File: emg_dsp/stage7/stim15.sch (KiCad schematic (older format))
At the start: 41 parts, among them U31 10X100, U32 MCP4017, U33 6533-CONN, U34 GT12MABE, U35 IL715-3, U36 IL715-3, U37 IL715-3, U38 IL715-3, U39 IL715-3, U40 IL715-3, U41 IL715-3, U42 IL715-3

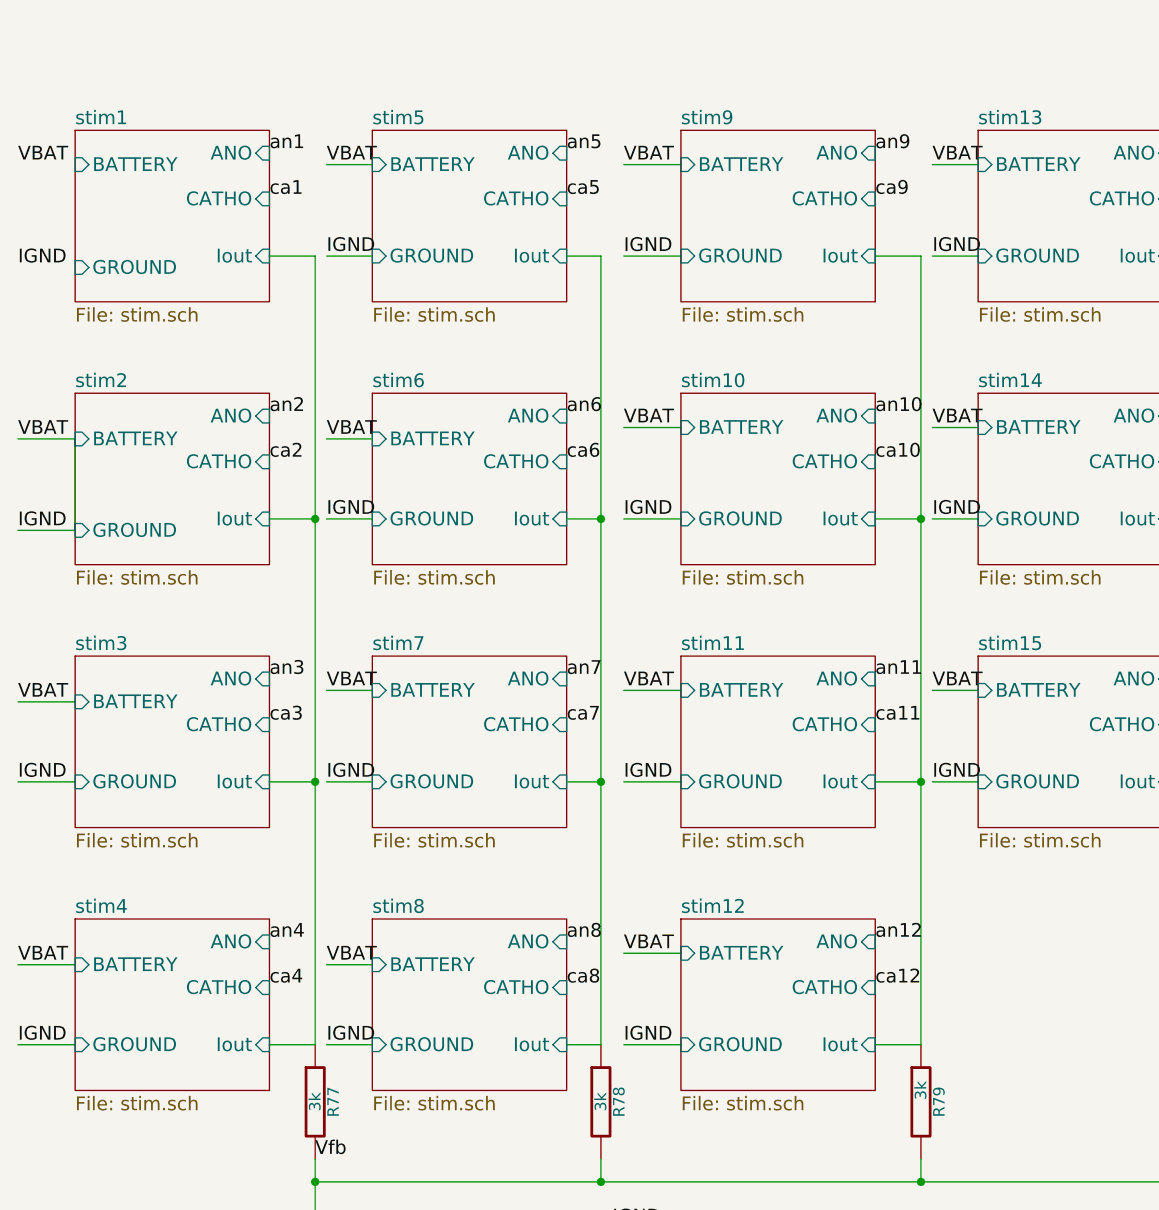
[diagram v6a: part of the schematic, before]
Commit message: finally fixed the VBAT = IGND issue - did so by using wires rather than labels on the inputs to the individual instances of stim.sch yea, that doesn't make sense -should work either way - but ok!
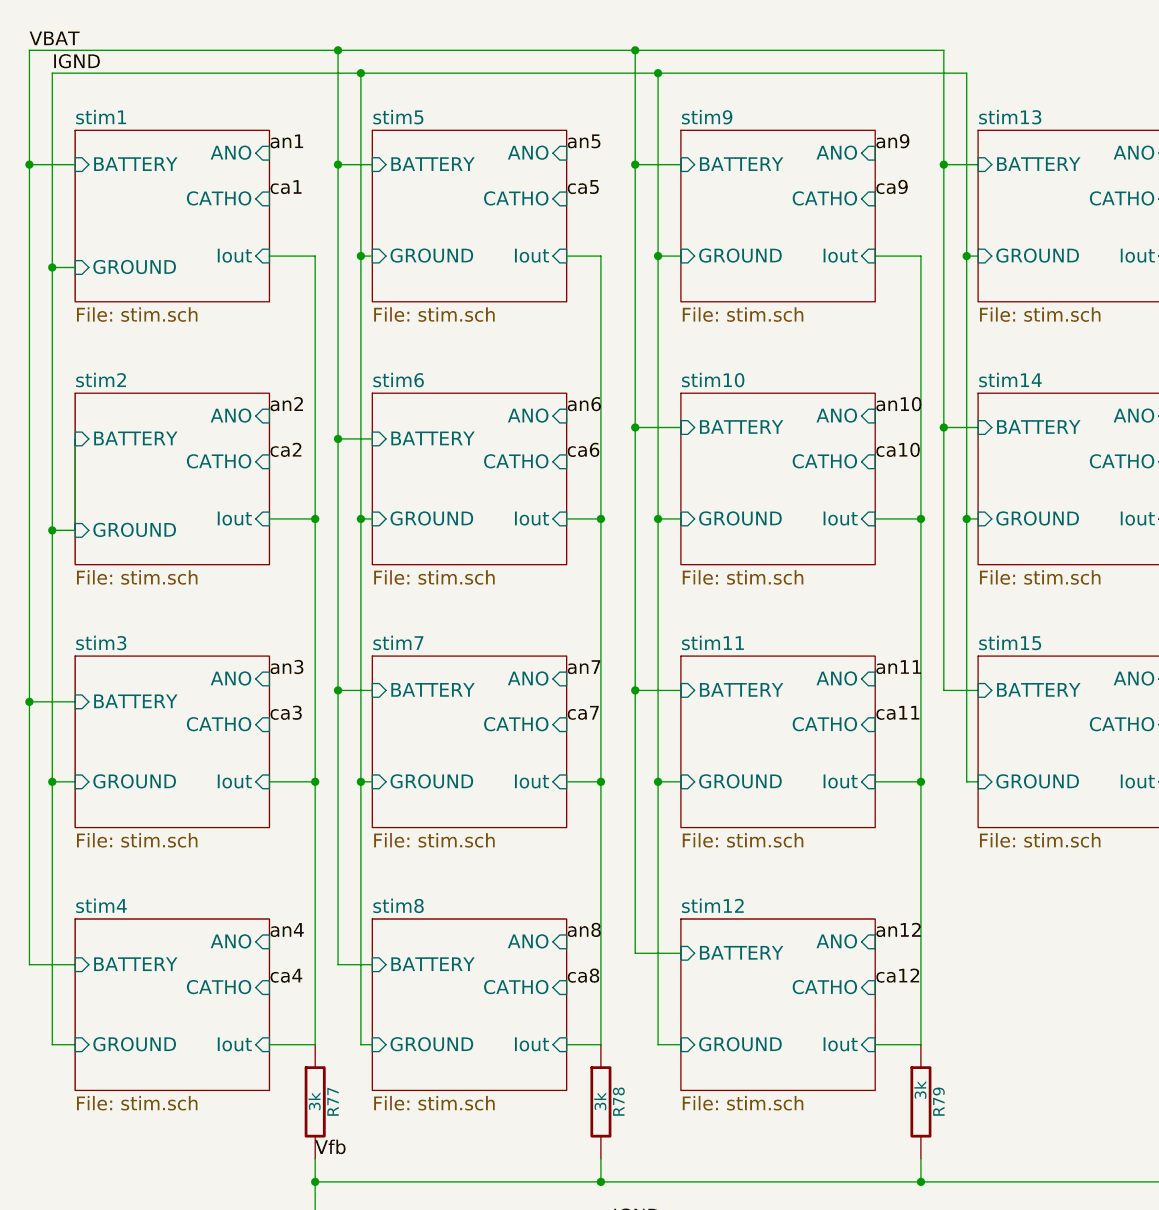
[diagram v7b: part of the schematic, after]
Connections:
- wire segments 259 -> 270
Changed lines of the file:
@@
-EESchema Schematic File Version 2  date Mon 24 Jan 2011 02:31:03 PM EST
+EESchema Schematic File Version 2  date Mon 24 Jan 2011 03:09:10 PM EST
 LIBS:power
 LIBS:device
@@
 Comment4 ""
 $EndDescr
+Text Label 800  1100 0    60   ~ 0
+IGND
+Text Label 700  1000 0    60   ~ 0
+VBAT
+Connection ~ 2050 1500
+Connection ~ 2050 1000
+Wire Wire Line
+	2050 1000 2050 5000
+Connection ~ 3350 1500
+Connection ~ 3350 1000
+Wire Wire Line
+	3350 1000 3350 4950
+Connection ~ 800  1950
+Connection ~ 4800 1900
+Wire Wire Line
+	4800 1100 4800 4200
+Wire Wire Line
+	4800 1100 800  1100
+Wire Wire Line
+	800  1100 800  5350
+Connection ~ 4800 3050
+Wire Wire Line
+	4850 3050 4800 3050
+Connection ~ 4700 2650
+Wire Wire Line
+	4850 2650 4700 2650
+Connection ~ 3450 3050
+Wire Wire Line
+	3550 3050 3450 3050
+Wire Wire Line
+	3550 5350 3450 5350
+Wire Wire Line
+	3450 1900 3550 1900
+Connection ~ 3350 2650
+Wire Wire Line
+	3550 2650 3350 2650
+Wire Wire Line
+	3350 1500 3550 1500
+Connection ~ 2150 4200
+Wire Wire Line
+	2200 4200 2150 4200
+Connection ~ 2050 2700
+Wire Wire Line
+	2200 2700 2050 2700
+Wire Wire Line
+	2050 5000 2200 5000
+Wire Wire Line
+	2050 1500 2200 1500
+Connection ~ 800  3100
+Wire Wire Line
+	800  3100 900  3100
+Wire Wire Line
+	800  5350 900  5350
+Wire Wire Line
+	800  1950 900  1950
 Connection ~ 7550 3000
 Wire Wire Line
@@
 Wire Wire Line
 	5000 6800 4750 6800
-Wire Wire Line
-	650  2700 900  2700
-Wire Wire Line
-	650  4200 900  4200
-Wire Wire Line
-	650  5350 900  5350
-Wire Wire Line
-	2200 5000 2000 5000
-Wire Wire Line
-	2200 3800 2000 3800
-Wire Wire Line
-	2200 2700 2000 2700
-Wire Wire Line
-	2200 1500 2000 1500
-Wire Wire Line
-	3550 4950 3300 4950
-Wire Wire Line
-	3550 3800 3300 3800
-Wire Wire Line
-	3550 2650 3300 2650
-Wire Wire Line
-	3550 1500 3300 1500
-Wire Wire Line
-	4850 1900 4650 1900
-Wire Wire Line
-	4850 3050 4650 3050
-Wire Wire Line
-	4850 4200 4650 4200
 Wire Wire Line
 	2000 6700 2200 6700
@@
 	3250 6550 3050 6550
 Wire Wire Line
-	900  2700 900  3100
-Wire Wire Line
-	4850 3800 4650 3800
-Wire Wire Line
-	4850 2650 4650 2650
-Wire Wire Line
-	4850 1500 4650 1500
-Wire Wire Line
-	3550 1900 3300 1900
-Wire Wire Line
-	3550 3050 3300 3050
-Wire Wire Line
-	3550 4200 3300 4200
-Wire Wire Line
-	3550 5350 3300 5350
-Wire Wire Line
-	2200 1900 2000 1900
-Wire Wire Line
-	2200 3050 2000 3050
-Wire Wire Line
-	2200 4200 2000 4200
-Wire Wire Line
-	2200 5350 2000 5350
-Wire Wire Line
-	900  5000 650  5000
-Wire Wire Line
-	900  3850 650  3850
-Wire Wire Line
-	900  3100 650  3100
+	900  3100 900  2700
 Wire Wire Line
 	4750 7350 4750 7100
@@
 Connection ~ 7750 8100
 Connection ~ 7950 8100
+Wire Wire Line
+	700  1500 900  1500
+Wire Wire Line
+	900  5000 700  5000
+Wire Wire Line
+	900  4200 800  4200
+Connection ~ 800  4200
+Wire Wire Line
+	900  3850 700  3850
+Connection ~ 700  3850
+Wire Wire Line
+	2200 3800 2050 3800
+Connection ~ 2050 3800
+Wire Wire Line
+	2150 1900 2200 1900
+Wire Wire Line
+	2200 5350 2150 5350
+Wire Wire Line
+	2200 3050 2150 3050
+Connection ~ 2150 3050
+Wire Wire Line
+	3550 3800 3350 3800
+Connection ~ 3350 3800
+Wire Wire Line
+	3350 4950 3550 4950
+Wire Wire Line
+	3550 4200 3450 4200
+Connection ~ 3450 4200
+Wire Wire Line
+	4700 1500 4850 1500
+Wire Wire Line
+	4850 3800 4700 3800
+Wire Wire Line
+	4800 1900 4850 1900
+Wire Wire Line
+	4800 4200 4850 4200
+Wire Wire Line
+	700  5000 700  1000
+Wire Wire Line
+	700  1000 4700 1000
+Wire Wire Line
+	4700 1000 4700 3800
+Connection ~ 4700 1500
+Connection ~ 700  1500
+Wire Wire Line
+	3450 5350 3450 1100
+Connection ~ 3450 1100
+Connection ~ 3450 1900
+Wire Wire Line
+	2150 5350 2150 1100
+Connection ~ 2150 1100
+Connection ~ 2150 1900
 Text Label 7950 9250 0    60   ~ 0
 VBAT
 Text Label 8300 9950 0    60   ~ 0
-IGND
-Text Label 650  1500 0    60   ~ 0
-VBAT
-Text Label 650  1950 0    60   ~ 0
 IGND
 $Sheet
@@
 	1    0    0    -1
 $EndComp
-Text Label 4650 4200 0    60   ~ 0
-IGND
-Text Label 4650 3050 0    60   ~ 0
-IGND
-Text Label 4650 1900 0    60   ~ 0
-IGND
-Text Label 3300 1900 0    60   ~ 0
-IGND
-Text Label 3300 3050 0    60   ~ 0
-IGND
-Text Label 3300 4200 0    60   ~ 0
-IGND
-Text Label 3300 5350 0    60   ~ 0
-IGND
-Text Label 2000 5350 0    60   ~ 0
-IGND
-Text Label 2000 4200 0    60   ~ 0
-IGND
-Text Label 2000 3050 0    60   ~ 0
-IGND
-Text Label 4650 3800 0    60   ~ 0
-VBAT
-Text Label 4650 2650 0    60   ~ 0
-VBAT
-Text Label 4650 1500 0    60   ~ 0
-VBAT
-Text Label 3300 4950 0    60   ~ 0
-VBAT
-Text Label 3300 3800 0    60   ~ 0
-VBAT
-Text Label 3300 2650 0    60   ~ 0
-VBAT
-Text Label 3300 1500 0    60   ~ 0
-VBAT
-Text Label 2000 5000 0    60   ~ 0
-VBAT
-Text Label 2000 3800 0    60   ~ 0
-VBAT
-Text Label 2000 2700 0    60   ~ 0
-VBAT
-Text Label 2000 1900 0    60   ~ 0
-IGND
-Text Label 2000 1500 0    60   ~ 0
-VBAT
-Text Label 650  5350 0    60   ~ 0
-IGND
-Text Label 650  5000 0    60   ~ 0
-VBAT
-Text Label 650  4200 0    60   ~ 0
-IGND
-Text Label 650  3850 0    60   ~ 0
-VBAT
-Text Label 650  3100 0    60   ~ 0
-IGND
-Text Label 650  2700 0    60   ~ 0
-VBAT
 Text Label 3250 6550 0    60   ~ 0
 VBAT
